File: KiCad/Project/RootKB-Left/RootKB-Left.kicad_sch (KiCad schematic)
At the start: 69 parts, among them J1 OLED-128x32, U1 Arduino_Pro_Micro, U2 TRRS

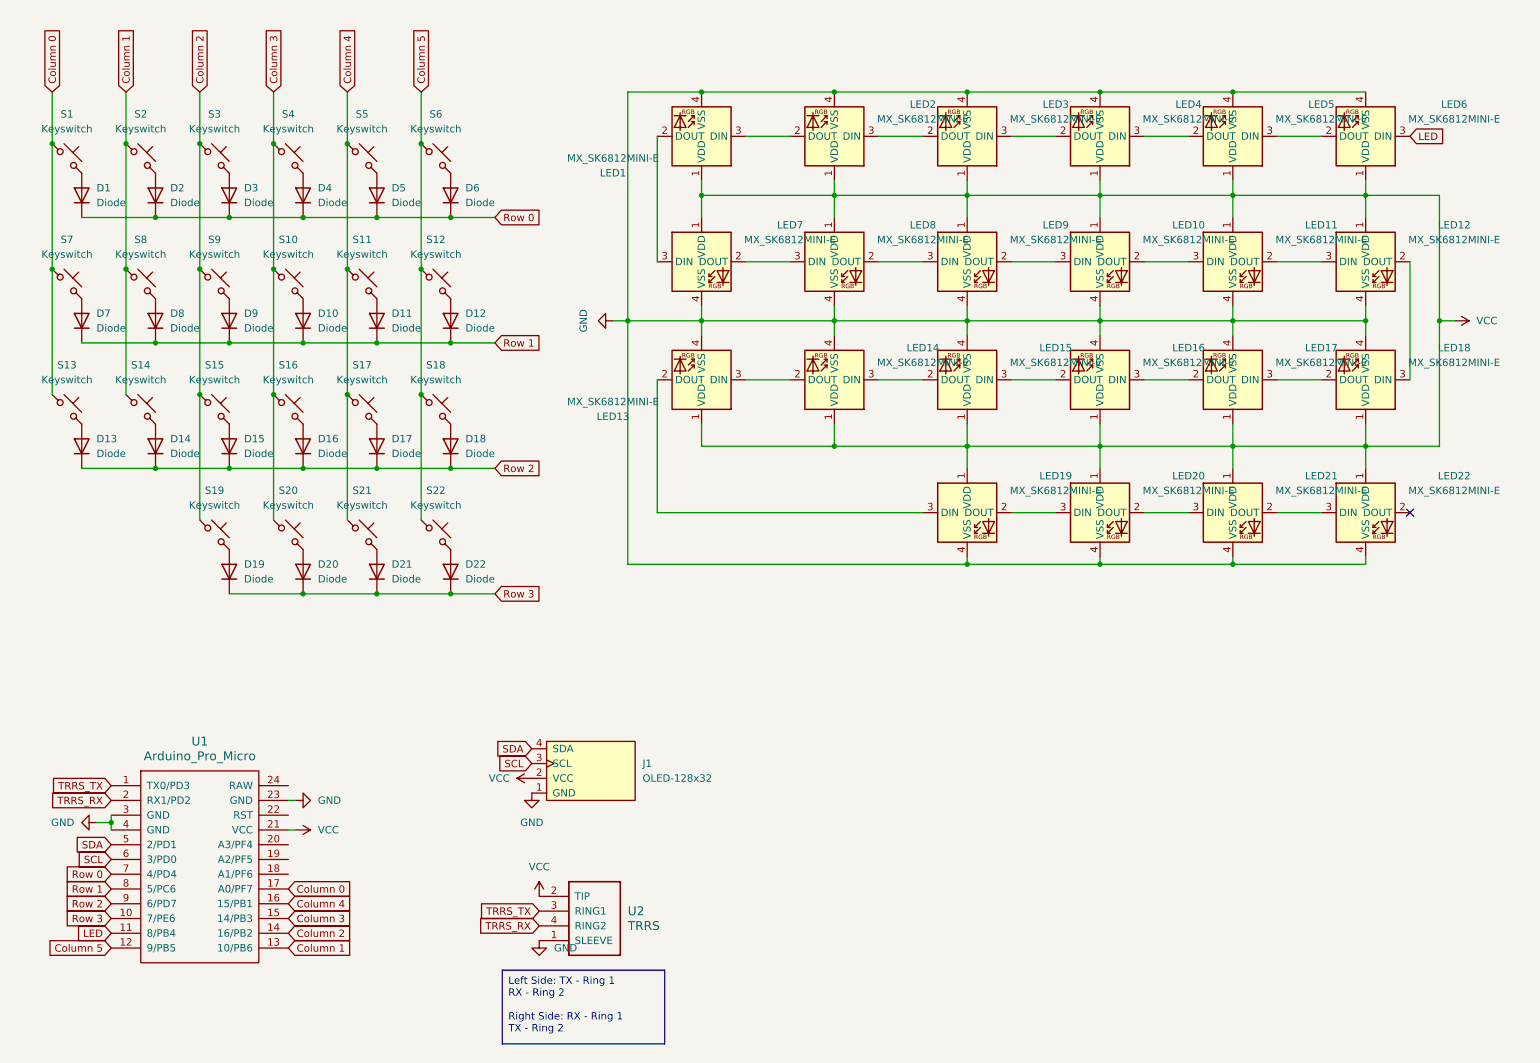
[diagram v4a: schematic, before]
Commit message: add titles
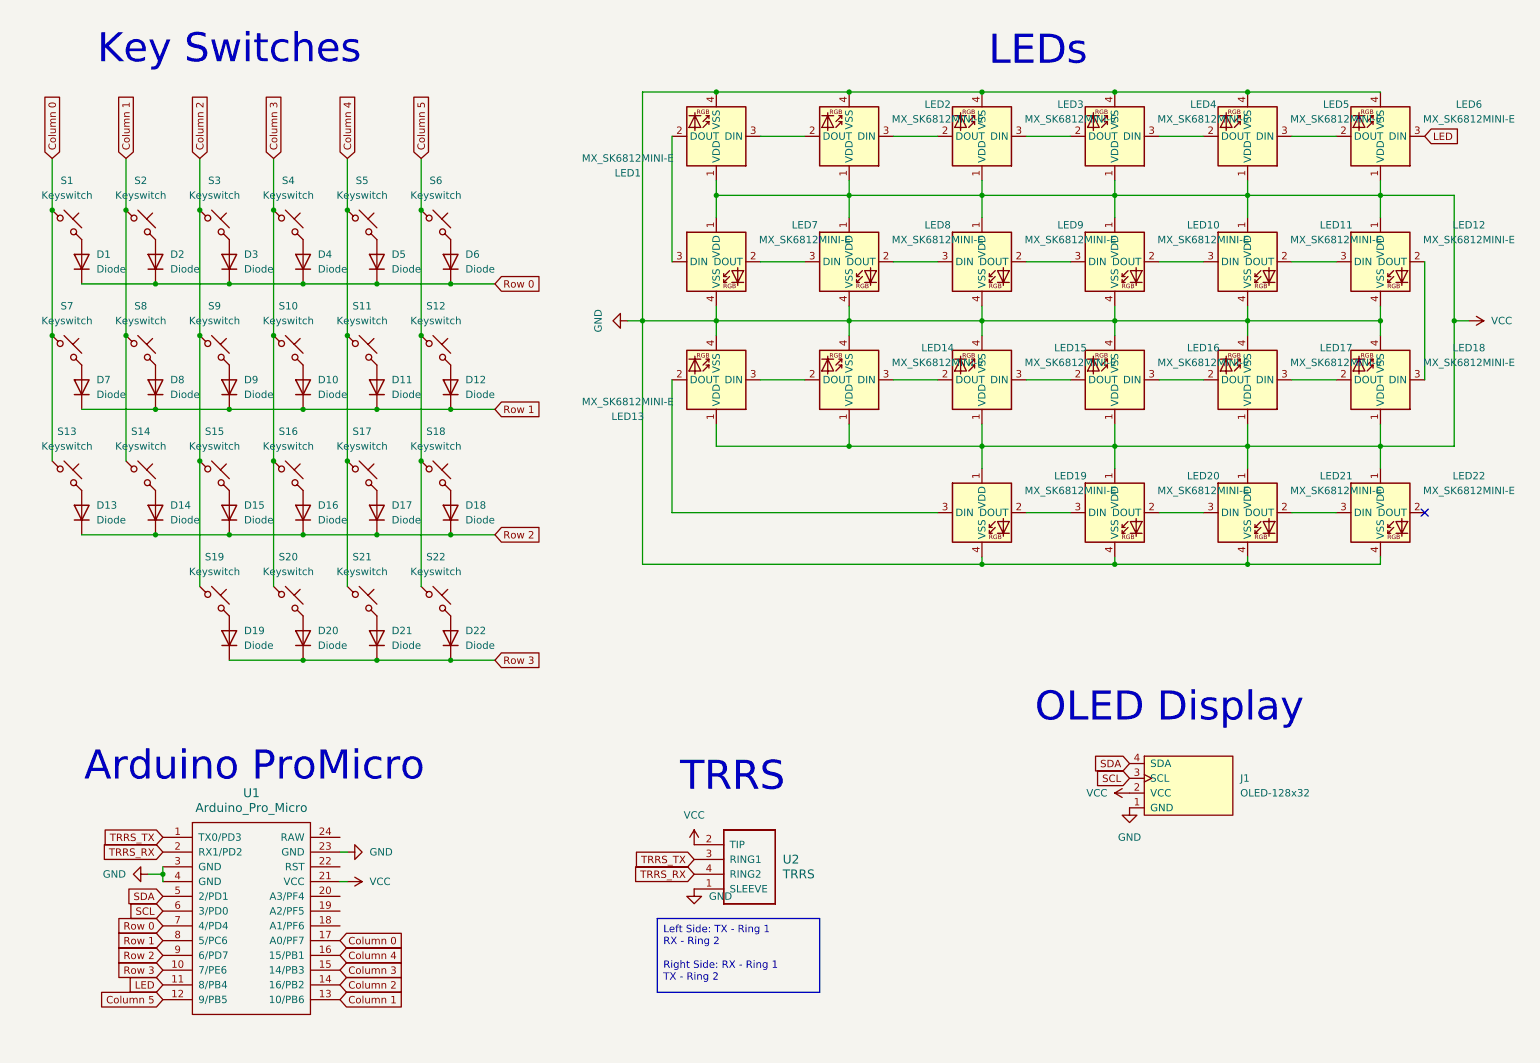
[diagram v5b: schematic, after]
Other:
- note added: "Arduino ProMicro"
- note added: "Key Switches"
- note added: "LEDs"
- note added: "OLED Display"
- note added: "TRRS"
- title: RootKB -> RootKB-Left
- moved on the sheet: D1, D10, D11, D12, D13, D14, D15, D16, D17, D18, D19, D2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
